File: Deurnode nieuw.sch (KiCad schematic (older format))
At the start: 37 parts, among them J1 EXT1, J10 Jumper Output, J11 Jumper Rel./Fet, J12 Screw_Terminal_01x03, J13 Screw_Terminal_01x03, J14 Screw_Terminal_01x02, J15 Screw_Terminal_01x02, J16 Conn_01x02, J17 Conn_01x02, J2 EXT2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

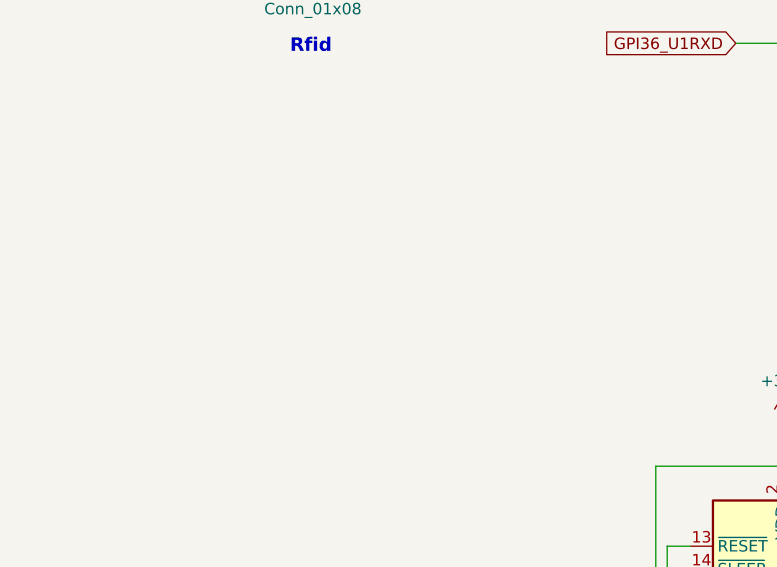
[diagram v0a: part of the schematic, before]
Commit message: DC-DC converter 12V -> 5V added to concept version 0.3
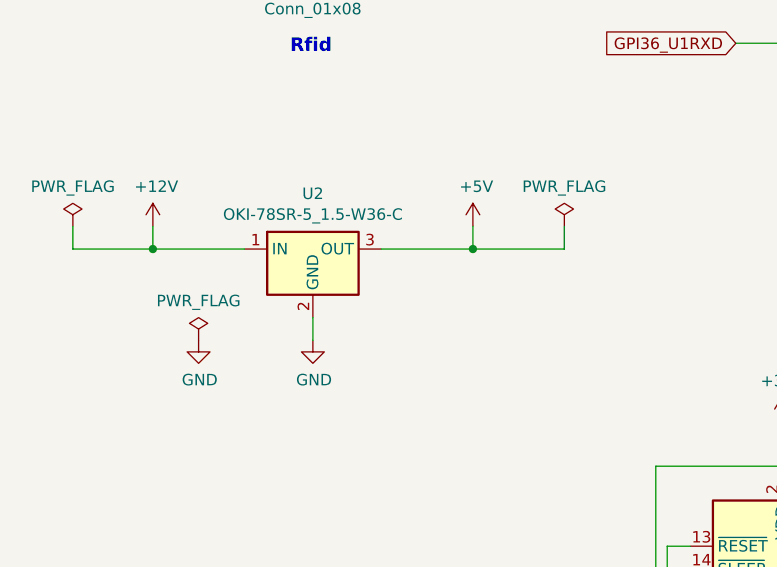
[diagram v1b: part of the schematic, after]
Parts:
- added U2: OKI-78SR-5_1.5-W36-C, Converter_DCDC:Converter_DCDC_muRata_OKI-78SR_Vertical, symbol Converter_DCDC:OKI-78SR-5_1.5-W36-C
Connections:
- net +12V: now also U2.1 (IN)
- net +5V: now also U2.3 (OUT)
- net GND: now also U2.2 (GND)
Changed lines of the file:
@@
 Sheet 1 1
 Title "Deurnode (based on Olimex ESP32-POE)"
-Date "2020-02-28"
-Rev "Version 0.2"
+Date "2020-03-02"
+Rev "Version 0.3"
 Comp "Makerspace Leiden"
 Comment1 "Hans Beerman"
@@
 Text Notes 8550 2050 0    59   ~ 12
 FET output
+$Comp
+L Converter_DCDC:OKI-78SR-5_1.5-W36-C U2
+U 1 1 5E5D0A07
+P 2500 4400
+F 0 "U2" H 2500 4642 50  0000 C CNN
+F 1 "OKI-78SR-5_1.5-W36-C" H 2500 4551 50  0000 C CNN
+F 2 "Converter_DCDC:Converter_DCDC_muRata_OKI-78SR_Vertical" H 2550 4150 50  0001 L CIN
+F 3 "https://power.murata.com/data/power/oki-78sr.pdf" H 2500 4400 50  0001 C CNN
+	1    2500 4400
+	1    0    0    -1
+$EndComp
+$Comp
+L power:GND #PWR021
+U 1 1 5E5D1D45
+P 2500 4800
+F 0 "#PWR021" H 2500 4550 50  0001 C CNN
+F 1 "GND" H 2505 4627 50  0000 C CNN
+F 2 "" H 2500 4800 50  0001 C CNN
+F 3 "" H 2500 4800 50  0001 C CNN
+	1    2500 4800
+	1    0    0    -1
+$EndComp
+$Comp
+L power:+12V #PWR020
+U 1 1 5E5D209E
+P 1800 4300
+F 0 "#PWR020" H 1800 4150 50  0001 C CNN
+F 1 "+12V" H 1815 4473 50  0000 C CNN
+F 2 "" H 1800 4300 50  0001 C CNN
+F 3 "" H 1800 4300 50  0001 C CNN
+	1    1800 4300
+	1    0    0    -1
+$EndComp
+Wire Wire Line
+	1800 4300 1800 4400
+Wire Wire Line
+	1800 4400 2200 4400
+Wire Wire Line
+	2500 4700 2500 4800
+Wire Wire Line
+	2800 4400 3200 4400
+$Comp
+L power:PWR_FLAG #FLG01
+U 1 1 5E62BB13
+P 1450 4300
+F 0 "#FLG01" H 1450 4375 50  0001 C CNN
+F 1 "PWR_FLAG" H 1450 4473 50  0000 C CNN
+F 2 "" H 1450 4300 50  0001 C CNN
+F 3 "~" H 1450 4300 50  0001 C CNN
+	1    1450 4300
+	1    0    0    -1
+$EndComp
+Wire Wire Line
+	1450 4300 1450 4400
+Wire Wire Line
+	1450 4400 1800 4400
+Connection ~ 1800 4400
+$Comp
+L power:PWR_FLAG #FLG03
+U 1 1 5E63CD5D
+P 3600 4300
+F 0 "#FLG03" H 3600 4375 50  0001 C CNN
+F 1 "PWR_FLAG" H 3600 4473 50  0000 C CNN
+F 2 "" H 3600 4300 50  0001 C CNN
+F 3 "~" H 3600 4300 50  0001 C CNN
+	1    3600 4300
+	1    0    0    -1
+$EndComp
+$Comp
+L power:+5V #PWR023
+U 1 1 5E63E8A4
+P 3200 4300
+F 0 "#PWR023" H 3200 4150 50  0001 C CNN
+F 1 "+5V" H 3215 4473 50  0000 C CNN
+F 2 "" H 3200 4300 50  0001 C CNN
+F 3 "" H 3200 4300 50  0001 C CNN
+	1    3200 4300
+	1    0    0    -1
+$EndComp
+Wire Wire Line
+	3200 4300 3200 4400
+Wire Wire Line
+	3200 4400 3600 4400
+Wire Wire Line
+	3600 4400 3600 4300
+Connection ~ 3200 4400
+$Comp
+L power:PWR_FLAG #FLG02
+U 1 1 5E64E3BA
+P 2000 4800
+F 0 "#FLG02" H 2000 4875 50  0001 C CNN
+F 1 "PWR_FLAG" H 2000 4973 50  0000 C CNN
+F 2 "" H 2000 4800 50  0001 C CNN
+F 3 "~" H 2000 4800 50  0001 C CNN
+	1    2000 4800
+	1    0    0    -1
+$EndComp
+$Comp
+L power:GND #PWR022
+U 1 1 5E64F961
+P 2000 4800
+F 0 "#PWR022" H 2000 4550 50  0001 C CNN
+F 1 "GND" H 2005 4627 50  0000 C CNN
+F 2 "" H 2000 4800 50  0001 C CNN
+F 3 "" H 2000 4800 50  0001 C CNN
+	1    2000 4800
+	1    0    0    -1
+$EndComp
 $EndSCHEMATC

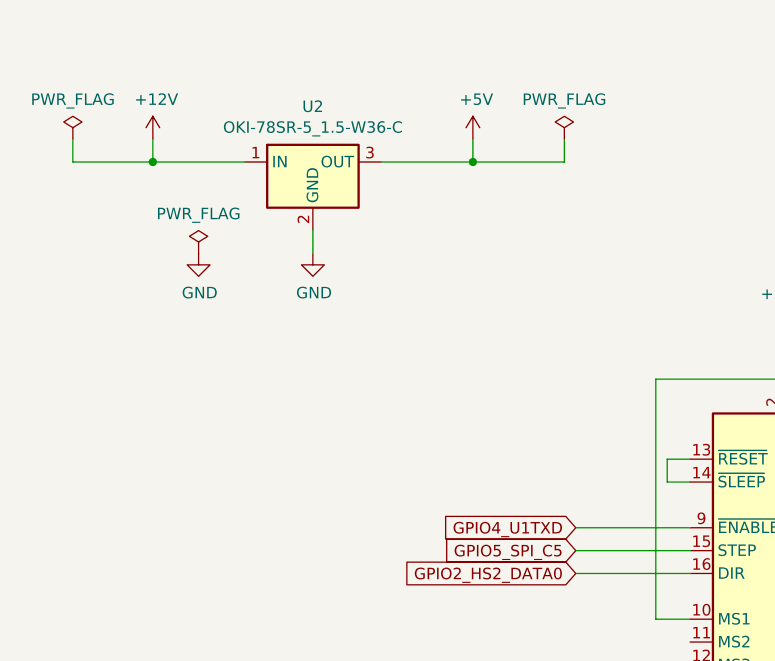
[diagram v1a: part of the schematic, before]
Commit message: README.md and other docs added, additional 12V connector added to design concept version 0.4
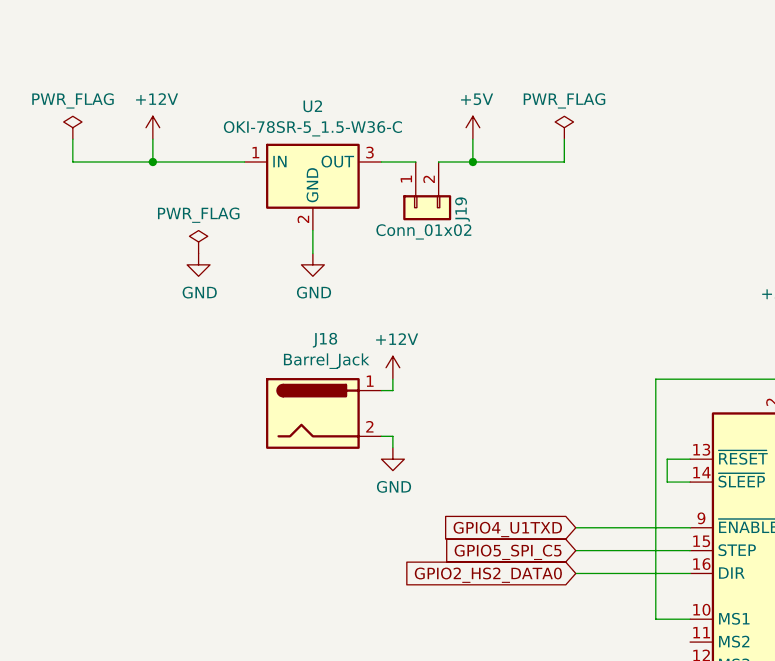
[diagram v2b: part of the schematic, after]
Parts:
- added J18: Barrel_Jack, Connector_BarrelJack:BarrelJack_CUI_PJ-063AH_Horizontal_CircularHoles, symbol Connector:Barrel_Jack
- added J19: Conn_01x02, Connector_PinHeader_2.54mm:PinHeader_1x02_P2.54mm_Vertical, symbol Connector_Generic:Conn_01x02
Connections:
- net +12V: now also J18.1
- net +5V: now also J19.2 (Pin_2); no longer U2.3 (OUT)
- net GND: now also J18.2
- new net: J19.1 (Pin_1), U2.3 (OUT)
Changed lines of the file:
@@
 Wire Wire Line
 	2500 4700 2500 4800
-Wire Wire Line
-	2800 4400 3200 4400
 $Comp
 L power:PWR_FLAG #FLG01
@@
 Wire Wire Line
 	3600 4400 3600 4300
-Connection ~ 3200 4400
 $Comp
 L power:PWR_FLAG #FLG02
@@
 	1    0    0    -1
 $EndComp
+$Comp
+L Connector:Barrel_Jack J18
+U 1 1 5E5DAF0A
+P 2500 5500
+F 0 "J18" H 2557 5825 50  0000 C CNN
+F 1 "Barrel_Jack" H 2557 5734 50  0000 C CNN
+F 2 "Connector_BarrelJack:BarrelJack_CUI_PJ-063AH_Horizontal_CircularHoles" H 2550 5460 50  0001 C CNN
+F 3 "~" H 2550 5460 50  0001 C CNN
+	1    2500 5500
+	1    0    0    -1
+$EndComp
+$Comp
+L power:+12V #PWR024
+U 1 1 5E5E3E19
+P 2850 5350
+F 0 "#PWR024" H 2850 5200 50  0001 C CNN
+F 1 "+12V" H 2865 5523 50  0000 C CNN
+F 2 "" H 2850 5350 50  0001 C CNN
+F 3 "" H 2850 5350 50  0001 C CNN
+	1    2850 5350
+	1    0    0    -1
+$EndComp
+$Comp
+L power:GND #PWR025
+U 1 1 5E5E43FB
+P 2850 5650
+F 0 "#PWR025" H 2850 5400 50  0001 C CNN
+F 1 "GND" H 2855 5477 50  0000 C CNN
+F 2 "" H 2850 5650 50  0001 C CNN
+F 3 "" H 2850 5650 50  0001 C CNN
+	1    2850 5650
+	1    0    0    -1
+$EndComp
+Wire Wire Line
+	2800 5400 2850 5400
+Wire Wire Line
+	2850 5400 2850 5350
+Wire Wire Line
+	2800 5600 2850 5600
+Wire Wire Line
+	2850 5600 2850 5650
+$Comp
+L Connector_Generic:Conn_01x02 J19
+U 1 1 5E5DCC3F
+P 2950 4600
+F 0 "J19" H 2900 4400 50  0000 L CNN
+F 1 "Conn_01x02" V 3050 4350 50  0000 L CNN
+F 2 "Connector_PinHeader_2.54mm:PinHeader_1x02_P2.54mm_Vertical" H 2950 4600 50  0001 C CNN
+F 3 "~" H 2950 4600 50  0001 C CNN
+	1    2950 4600
+	0    -1   1    0
+$EndComp
+Wire Wire Line
+	2800 4400 2950 4400
+Wire Wire Line
+	3050 4400 3200 4400
+Connection ~ 3200 4400
 $EndSCHEMATC
